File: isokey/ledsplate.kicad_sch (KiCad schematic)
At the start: 155 parts

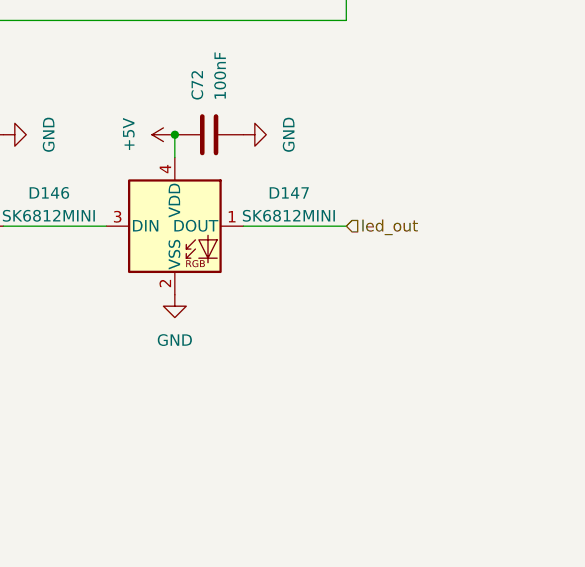
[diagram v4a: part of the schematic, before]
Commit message: Complete led wire
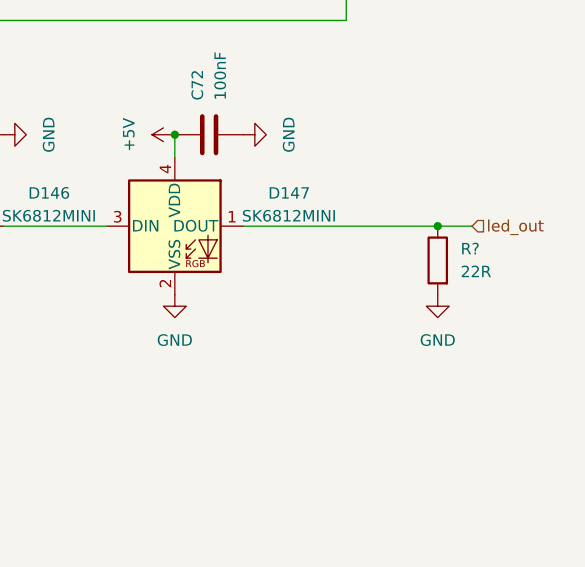
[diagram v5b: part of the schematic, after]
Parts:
- added R?: 22R, Resistor_SMD:R_0603_1608Metric_Pad0.98x0.95mm_HandSolder, symbol Device:R
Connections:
- net GND: now also R?.2
- net led_out: now also R?.1
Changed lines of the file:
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@@
   (junction (at 270.51 24.13) (diameter 0) (color 0 0 0 0)
   )
+  (junction (at 379.73 233.68) (diameter 0) (color 0 0 0 0)
+  )
   (junction (at 49.53 182.88) (diameter 0) (color 0 0 0 0)
   )
@@
     (stroke (width 0) (type default))
   )
+  (wire (pts (xy 379.73 233.68) (xy 383.54 233.68))
+    (stroke (width 0) (type default))
+  )
   (wire (pts (xy 134.62 182.88) (xy 134.62 185.42))
     (stroke (width 0) (type default))
@@
     (stroke (width 0) (type default))
   )
+  (wire (pts (xy 358.14 233.68) (xy 379.73 233.68))
+    (stroke (width 0) (type default))
+  )
   (wire (pts (xy 113.03 152.4) (xy 127 152.4))
     (stroke (width 0) (type default))
@@
     (stroke (width 0) (type default))
   )
-  (wire (pts (xy 358.14 233.68) (xy 369.57 233.68))
-    (stroke (width 0) (type default))
-  )
   (wire (pts (xy 168.91 152.4) (xy 182.88 152.4))
     (stroke (width 0) (type default))
@@
     (effects (font (size 1.27 1.27)) (justify left))
   )
-  (hierarchical_label "led_out" (shape input) (at 369.57 233.68 0) (fields_autoplaced)
+  (hierarchical_label "led_out" (shape input) (at 383.54 233.68 0) (fields_autoplaced)
     (effects (font (size 1.27 1.27)) (justify left))
   )
@@
     )
   )
+  (symbol (lib_id "Device:R") (at 379.73 237.49 0) (mirror y) (unit 1)
+    (in_bom yes) (on_board yes) (dnp no) (fields_autoplaced)
+    (property "Reference" "R?" (at 382.27 236.22 0)
+      (effects (font (size 1.27 1.27)) (justify right))
+    )
+    (property "Value" "22R" (at 382.27 238.76 0)
+      (effects (font (size 1.27 1.27)) (justify right))
+    )
+    (property "Footprint" "Resistor_SMD:R_0603_1608Metric_Pad0.98x0.95mm_HandSolder" (at 381.508 237.49 90)
+      (effects (font (size 1.27 1.27)) hide)
+    )
+    (property "Datasheet" "~" (at 379.73 237.49 0)
+      (effects (font (size 1.27 1.27)) hide)
+    )
+    (pin "1")
+    (pin "2")
+    (instances
+      (project "isokey"
+        (path "/b0c352a4-2db1-45ff-8668-f2efdeb7d408/fdcf2c12-f432-4cc9-a99f-9b8019eb8ce2"
+          (reference "R?") (unit 1)
+        )
+        (path "/b0c352a4-2db1-45ff-8668-f2efdeb7d408/870755d2-ff44-4c69-82b3-4018370ecd52"
+          (reference "R22") (unit 1)
+        )
+      )
+    )
+  )
   (symbol (lib_id "power:GND") (at 95.25 259.08 90) (unit 1)
     (in_bom yes) (on_board yes) (dnp no) (fields_autoplaced)
@@
         )
       )
+    )
+  )
+  (symbol (lib_id "power:GND") (at 379.73 241.3 0) (unit 1)
+    (in_bom yes) (on_board yes) (dnp no) (fields_autoplaced)
+    (property "Reference" "#PWR0238" (at 379.73 247.65 0)
+      (effects (font (size 1.27 1.27)) hide)
+    )
+    (property "Value" "GND" (at 379.73 246.38 0)
+      (effects (font (size 1.27 1.27)))
+    )
+    (property "Footprint" "" (at 379.73 241.3 0)
+      (effects (font (size 1.27 1.27)) hide)
+    )
+    (property "Datasheet" "" (at 379.73 241.3 0)
+      (effects (font (size 1.27 1.27)) hide)
+    )
+    (pin "1")
+    (instances
+      (project "isokey"
+        (path "/b0c352a4-2db1-45ff-8668-f2efdeb7d408/870755d2-ff44-4c69-82b3-4018370ecd52"
+          (reference "#PWR0238") (unit 1)
+        )
+      )

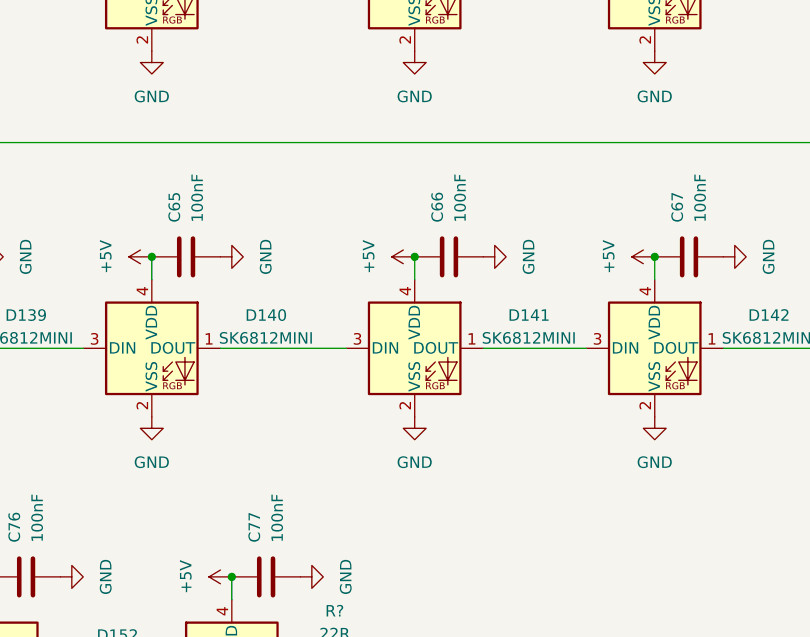
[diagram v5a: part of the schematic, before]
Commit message: Update scheme. Continue routing.
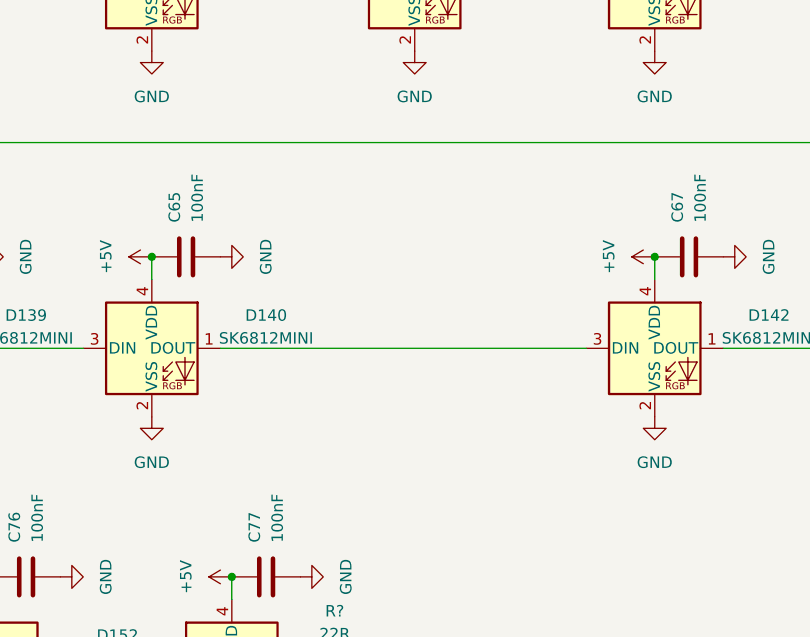
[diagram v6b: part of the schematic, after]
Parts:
- removed C66: 100nF, Capacitor_SMD:C_0603_1608Metric_Pad1.08x0.95mm_HandSolder, symbol Device:C
- removed D141: SK6812MINI, LED_SMD:LED_SK6812MINI_PLCC4_3.5x3.5mm_P1.75mm, symbol LED:SK6812MINI
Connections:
- net at D142.3 (DIN): now also D140.1 (DOUT)
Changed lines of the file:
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@@
   (junction (at 243.84 223.52) (diameter 0) (color 0 0 0 0)
   )
-  (junction (at 190.5 223.52) (diameter 0) (color 0 0 0 0)
-  )
   (junction (at 78.74 182.88) (diameter 0) (color 0 0 0 0)
   )
@@
     (stroke (width 0) (type default))
   )
-  (wire (pts (xy 190.5 223.52) (xy 190.5 226.06))
-    (stroke (width 0) (type default))
-  )
   (wire (pts (xy 113.03 73.66) (xy 127 73.66))
     (stroke (width 0) (type default))
@@
     (stroke (width 0) (type default))
   )
-  (wire (pts (xy 198.12 233.68) (xy 209.55 233.68))
+  (wire (pts (xy 168.91 233.68) (xy 209.55 233.68))
     (stroke (width 0) (type default))
   )
@@
     (stroke (width 0) (type default))
   )
-  (wire (pts (xy 168.91 233.68) (xy 182.88 233.68))
-    (stroke (width 0) (type default))
-  )
   (wire (pts (xy 170.18 259.08) (xy 170.18 261.62))
     (stroke (width 0) (type default))
@@
     )
   )
-  (symbol (lib_id "power:GND") (at 190.5 241.3 0) (unit 1)
-    (in_bom yes) (on_board yes) (dnp no) (fields_autoplaced)
-    (property "Reference" "#PWR0202" (at 190.5 247.65 0)
-      (effects (font (size 1.27 1.27)) hide)
-    )
-    (property "Value" "GND" (at 190.5 246.38 0)
-      (effects (font (size 1.27 1.27)))
-    )
-    (property "Footprint" "" (at 190.5 241.3 0)
-      (effects (font (size 1.27 1.27)) hide)
-    )
-    (property "Datasheet" "" (at 190.5 241.3 0)
-      (effects (font (size 1.27 1.27)) hide)
-    )
-    (pin "1")
-    (instances
-      (project "isokey"
-        (path "/b0c352a4-2db1-45ff-8668-f2efdeb7d408/870755d2-ff44-4c69-82b3-4018370ecd52"
-          (reference "#PWR0202") (unit 1)
-        )
-      )
-    )
-  )
   (symbol (lib_id "LED:SK6812MINI") (at 190.5 73.66 0) (unit 1)
     (in_bom yes) (on_board yes) (dnp no) (fields_autoplaced)
@@
     )
   )
-  (symbol (lib_id "power:GND") (at 198.12 223.52 90) (unit 1)
-    (in_bom yes) (on_board yes) (dnp no) (fields_autoplaced)
-    (property "Reference" "#PWR0184" (at 204.47 223.52 0)
-      (effects (font (size 1.27 1.27)) hide)
-    )
-    (property "Value" "GND" (at 203.2 223.52 0)
-      (effects (font (size 1.27 1.27)))
-    )
-    (property "Footprint" "" (at 198.12 223.52 0)
-      (effects (font (size 1.27 1.27)) hide)
-    )
-    (property "Datasheet" "" (at 198.12 223.52 0)
-      (effects (font (size 1.27 1.27)) hide)
-    )
-    (pin "1")
-    (instances
-      (project "isokey"
-        (path "/b0c352a4-2db1-45ff-8668-f2efdeb7d408/870755d2-ff44-4c69-82b3-4018370ecd52"
-          (reference "#PWR0184") (unit 1)
-        )
-      )
-    )
-  )
   (symbol (lib_id "power:+5V") (at 350.52 24.13 90) (unit 1)
     (in_bom yes) (on_board yes) (dnp no) (fields_autoplaced)
@@
     )
   )
-  (symbol (lib_id "Device:C") (at 194.31 223.52 90) (unit 1)
-    (in_bom yes) (on_board yes) (dnp no) (fields_autoplaced)
-    (property "Reference" "C66" (at 193.04 219.71 0)
-      (effects (font (size 1.27 1.27)) (justify left))
-    )
-    (property "Value" "100nF" (at 195.58 219.71 0)
-      (effects (font (size 1.27 1.27)) (justify left))
-    )
-    (property "Footprint" "Capacitor_SMD:C_0603_1608Metric_Pad1.08x0.95mm_HandSolder" (at 198.12 222.5548 0)
-      (effects (font (size 1.27 1.27)) hide)
-    )
-    (property "Datasheet" "~" (at 194.31 223.52 0)
-      (effects (font (size 1.27 1.27)) hide)
-    )
-    (pin "1")
-    (pin "2")
-    (instances
-      (project "isokey"
-        (path "/b0c352a4-2db1-45ff-8668-f2efdeb7d408/870755d2-ff44-4c69-82b3-4018370ecd52"
-          (reference "C66") (unit 1)
-        )
-      )
-    )
-  )
   (symbol (lib_id "power:GND") (at 86.36 101.6 90) (unit 1)
     (in_bom yes) (on_board yes) (dnp no) (fields_autoplaced)
@@
     )
   )
-  (symbol (lib_id "LED:SK6812MINI") (at 190.5 233.68 0) (unit 1)
-    (in_bom yes) (on_board yes) (dnp no) (fields_autoplaced)
-    (property "Reference" "D141" (at 203.2 230.0321 0)
-      (effects (font (size 1.27 1.27)))
-    )
-    (property "Value" "SK6812MINI" (at 203.2 232.5721 0)
-      (effects (font (size 1.27 1.27)))
-    )
-    (property "Footprint" "LED_SMD:LED_SK6812MINI_PLCC4_3.5x3.5mm_P1.75mm" (at 191.77 241.3 0)
-      (effects (font (size 1.27 1.27)) (justify left top) hide)
-    )
-    (property "Datasheet" "https://cdn-shop.adafruit.com/product-files/2686/SK6812MINI_REV.01-1-2.pdf" (at 193.04 243.205 0)
-      (effects (font (size 1.27 1.27)) (justify left top) hide)
-    )
-    (pin "1")
-    (pin "2")
-    (pin "3")
-    (pin "4")
-    (instances
-      (project "isokey"
-        (path "/b0c352a4-2db1-45ff-8668-f2efdeb7d408/870755d2-ff44-4c69-82b3-4018370ecd52"
-          (reference "D141") (unit 1)
-        )
-      )
-    )
-  )
   (symbol (lib_id "power:GND") (at 198.12 101.6 90) (unit 1)
     (in_bom yes) (on_board yes) (dnp no) (fields_autoplaced)
@@
         )
       )
-    )
-  )
-  (symbol (lib_id "power:+5V") (at 190.5 223.52 90) (unit 1)
-    (in_bom yes) (on_board yes) (dnp no) (fields_autoplaced)
-    (property "Reference" "#PWR0183" (at 194.31 223.52 0)
-      (effects (font (size 1.27 1.27)) hide)
-    )
-    (property "Value" "+5V" (at 185.42 223.52 0)
-      (effects (font (size 1.27 1.27)))
-    )
-    (property "Footprint" "" (at 190.5 223.52 0)
-      (effects (font (size 1.27 1.27)) hide)
-    )
-    (property "Datasheet" "" (at 190.5 223.52 0)
-      (effects (font (size 1.27 1.27)) hide)
-    )
-    (pin "1")
-    (instances
-      (project "isokey"
-        (path "/b0c352a4-2db1-45ff-8668-f2efdeb7d408/870755d2-ff44-4c69-82b3-4018370ecd52"
-          (reference "#PWR0183") (unit 1)
-        )
-      )

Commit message: WIP
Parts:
- removed C34, C45, C56, C57, C68, C77: 100nF, Capacitor_SMD:C_0603_1608Metric_Pad1.08x0.95mm_HandSolder, symbol Device:C
- removed D148, D149, D150, D151, D152: SK6812MINI, LED_SMD:LED_SK6812MINI_PLCC4_3.5x3.5mm_P1.75mm, symbol LED:SK6812MINI
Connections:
- net at D76.3 (DIN): now also R?.2

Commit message: isokey: start splitting
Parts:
- renumbered C1 to C14, C2 to C15, C3 to C16, C4 to C17, C5 to C18, C6 to C19, C7 to C20, C8 to C21, C9 to C22, C10 to C23, C11 to C24, C12 to C25, C13 to C26, C14 to C27, C15 to C28, C16 to C29, C17 to C30, C18 to C31, C19 to C32, C20 to C33, C21 to C34, C22 to C35, C23 to C36, C24 to C37, C25 to C38, C26 to C39, C27 to C40, C28 to C41, C29 to C42, C30 to C43, C31 to C44, C32 to C45, C33 to C46, C35 to C47, C36 to C48, C37 to C49, C38 to C50, C39 to C51, C40 to C52, C41 to C53, C42 to C54, C43 to C55, C44 to C56, C46 to C57, C47 to C58, C48 to C59, C49 to C60, C50 to C61, C51 to C62, C52 to C63, C53 to C64, C54 to C65, C55 to C66, C58 to C67, C59 to C68, C60 to C69, C61 to C70, C62 to C71, C63 to C72, C64 to C73, C65 to C74, C67 to C75, C69 to C76, C70 to C77, C71 to C78, C72 to C79, C73 to C80, C74 to C81, C75 to C82, C76 to C83, D147 to D100, D76 to D30, D77 to D31, D78 to D32, D79 to D33, D80 to D34, D81 to D35, D82 to D36, D83 to D37, D84 to D38, D85 to D39, D86 to D40, D87 to D41, D88 to D42, D89 to D43, D90 to D44, D91 to D45, D92 to D46, D93 to D47, D94 to D48, D95 to D49, D96 to D50, D97 to D51, D98 to D52, D99 to D53, D100 to D54, D101 to D55, D102 to D56, D103 to D57, D104 to D58, D105 to D59, D106 to D60, D107 to D61, D108 to D62, D109 to D63, D110 to D64, D111 to D65, D112 to D66, D113 to D67, D114 to D68, D115 to D69, D116 to D70, D117 to D71, D118 to D72, D119 to D73, D120 to D74, D121 to D75, D122 to D76, D123 to D77, D124 to D78, D125 to D79, D126 to D80, D127 to D81, D128 to D82, D129 to D83, D130 to D84, D131 to D85, D132 to D86, D133 to D87, D134 to D88, D135 to D89, D136 to D90, D137 to D91, D138 to D92, D139 to D93, D140 to D94, D142 to D95, D143 to D96, D144 to D97, D145 to D98, D146 to D99
